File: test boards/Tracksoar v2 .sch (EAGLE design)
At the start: 53 parts, among them IC1 BME280, Y1 16MHZ

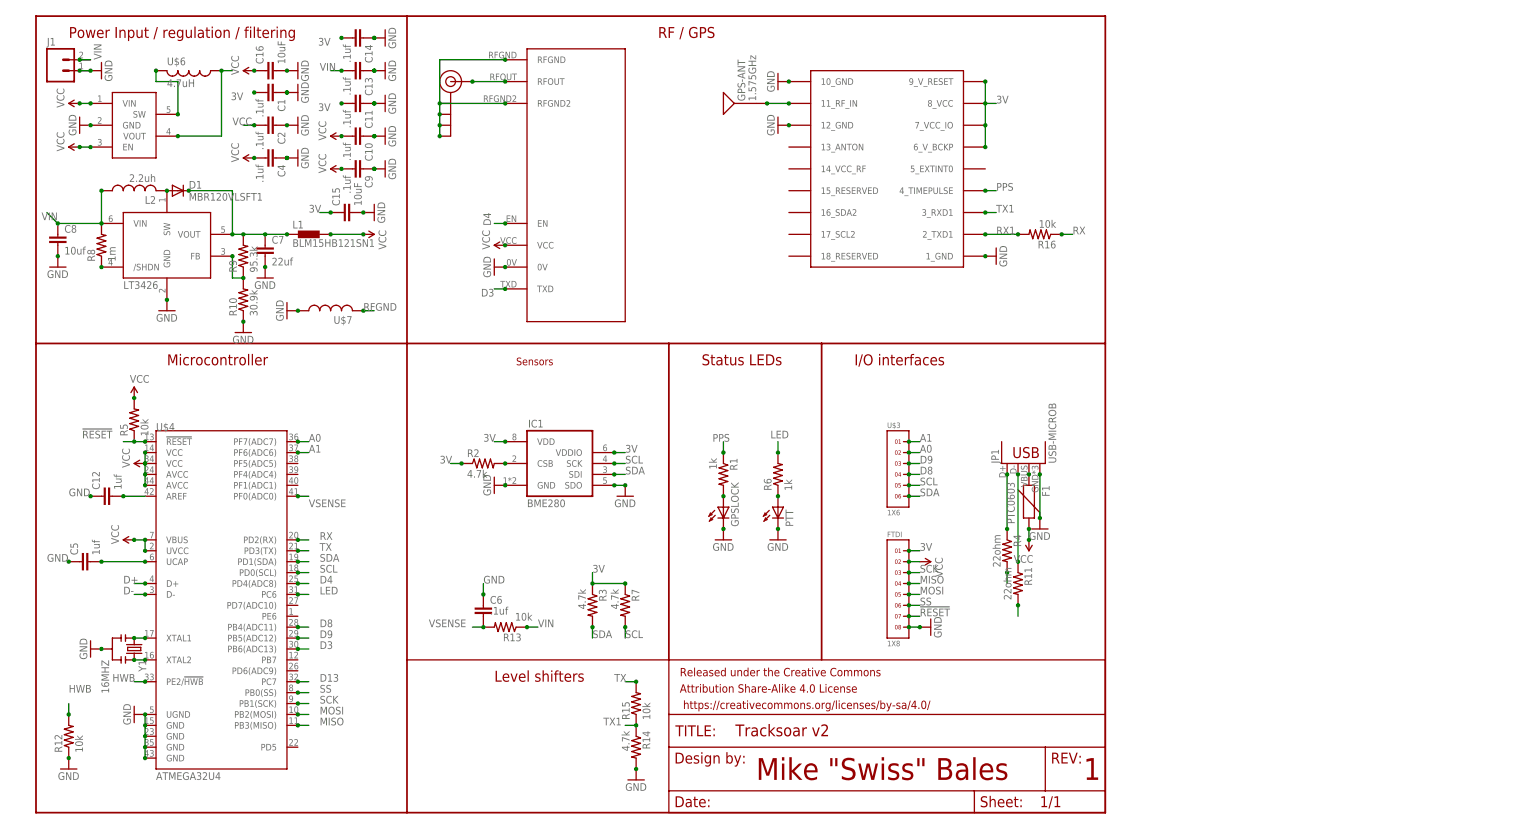
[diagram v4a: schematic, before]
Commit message: Added gps backup cap
added gps backup capacitor. Corrected serial voltage divider resistor values. Removed ground vias below gps module.
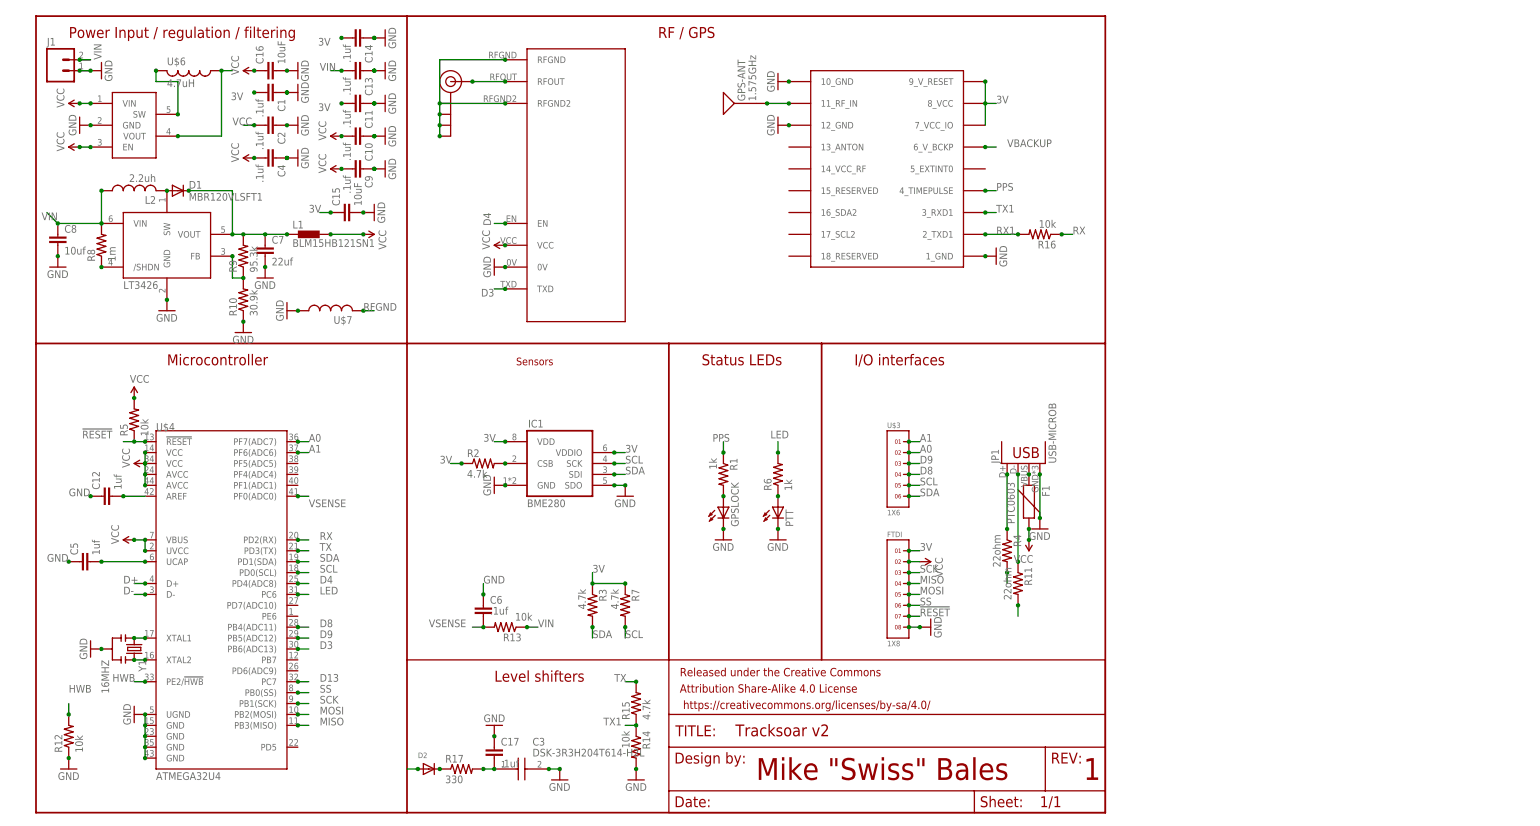
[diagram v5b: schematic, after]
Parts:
- added C17: .1uf, SparkFun-Capacitors:CAP0402-CAP
- added C3: DSK-3R3H204T614-H2L, DSK-3R3H204T614-H2L:DSK-3R3H204T614-H2L
- added D2: (no value), adafruit:DIODESOD-123
- added R17: 330, adafruit:R-US_R0402
- R14: value 4.7k -> 10k
- R15: value 10k -> 4.7k
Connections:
- new net N$22: D2.C, R17.1
- new net VBACKUP: C17.2, C3.+, R17.2, U$1.6_V_BCKP
- net 3V: now also D2.A; no longer U$1.6_V_BCKP
- net GND: now also C17.1, C3.-
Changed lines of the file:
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@@
 <part name="GND3" library="SparkFun-Aesthetics" deviceset="GND" device=""/>
 <part name="GND31" library="SparkFun-Aesthetics" deviceset="GND" device=""/>
-<part name="R14" library="adafruit" deviceset="R-US_" device="R0402" value="4.7k"/>
-<part name="R15" library="adafruit" deviceset="R-US_" device="R0402" value="10k"/>
+<part name="R14" library="adafruit" deviceset="R-US_" device="R0402" value="10k"/>
+<part name="R15" library="adafruit" deviceset="R-US_" device="R0402" value="4.7k"/>
 <part name="GND1" library="SparkFun-Aesthetics" deviceset="GND" device=""/>
 <part name="R16" library="adafruit" deviceset="R-US_" device="R0402" value="10k"/>
@@
 <part name="C2" library="SparkFun-Capacitors" deviceset="CAP" device="0402-CAP" value=".1uf"/>
 <part name="GND2" library="SparkFun-Aesthetics" deviceset="GND" device=""/>
+<part name="C3" library="DSK-3R3H204T614-H2L" deviceset="DSK-3R3H204T614-H2L" device=""/>
+<part name="D2" library="adafruit" library_urn="urn:adsk.eagle:library:420" deviceset="DIODE" device="SOD-123"/>
+<part name="R17" library="adafruit" deviceset="R-US_" device="R0402" value="330"/>
+<part name="C17" library="SparkFun-Capacitors" deviceset="CAP" device="0402-CAP" value=".1uf"/>
+<part name="GND4" library="SparkFun-Aesthetics" deviceset="GND" device=""/>
+<part name="GND33" library="SparkFun-Aesthetics" deviceset="GND" device=""/>
 </parts>
 <sheets>
@@
 <instance part="C2" gate="G$1" x="53.34" y="160.02" rot="R270"/>
 <instance part="GND2" gate="1" x="60.96" y="160.02" rot="R90"/>
+<instance part="C3" gate="G$1" x="106.68" y="10.16"/>
+<instance part="D2" gate="G$1" x="91.44" y="10.16"/>
+<instance part="R17" gate="G$1" x="99.06" y="10.16"/>
+<instance part="C17" gate="G$1" x="106.68" y="12.7"/>
+<instance part="GND4" gate="1" x="106.68" y="20.32" rot="R180"/>
+<instance part="GND33" gate="1" x="121.92" y="7.62"/>
 </instances>
 <busses>
@@
 <junction x="58.42" y="160.02"/>
 </segment>
+<segment>
+<pinref part="C3" gate="G$1" pin="-"/>
+<wire x1="119.38" y1="10.16" x2="121.92" y2="10.16" width="0.1524" layer="91"/>
+<junction x="119.38" y="10.16"/>
+<pinref part="GND33" gate="1" pin="GND"/>
+<junction x="121.92" y="10.16"/>
+</segment>
+<segment>
+<pinref part="C17" gate="G$1" pin="1"/>
+<pinref part="GND4" gate="1" pin="GND"/>
+<junction x="106.68" y="17.78"/>
+</segment>
 </net>
 <net name="D3" class="0">
@@
 <pinref part="U$1" gate="G$1" pin="7_VCC_IO"/>
 <wire x1="220.98" y1="170.18" x2="220.98" y2="165.1" width="0.1524" layer="91"/>
-<junction x="220.98" y="160.02"/>
 <junction x="220.98" y="165.1"/>
 <wire x1="220.98" y1="165.1" x2="220.98" y2="160.02" width="0.1524" layer="91"/>
 <junction x="220.98" y="170.18"/>
-<pinref part="U$1" gate="G$1" pin="6_V_BCKP"/>
-<wire x1="220.98" y1="160.02" x2="220.98" y2="154.94" width="0.1524" layer="91"/>
-<junction x="220.98" y="154.94"/>
 </segment>
 <segment>
@@
 <junction x="33.02" y="157.48"/>
 <junction x="43.18" y="172.72"/>
+</segment>
+<segment>
+<pinref part="D2" gate="G$1" pin="A"/>
+<wire x1="88.9" y1="10.16" x2="86.36" y2="10.16" width="0.1524" layer="91"/>
+<junction x="88.9" y="10.16"/>
 </segment>
 </net>
@@
 </segment>
 </net>
+<net name="VBACKUP" class="0">
+<segment>
+<pinref part="U$1" gate="G$1" pin="6_V_BCKP"/>
+<wire x1="220.98" y1="154.94" x2="223.52" y2="154.94" width="0.1524" layer="91"/>
+<label x="226.06" y="154.94" size="1.778" layer="95"/>
+<junction x="220.98" y="154.94"/>
+</segment>
+<segment>
+<pinref part="C3" gate="G$1" pin="+"/>
+<wire x1="106.68" y1="10.16" x2="104.14" y2="10.16" width="0.1524" layer="91"/>
+<junction x="106.68" y="10.16"/>
+<pinref part="R17" gate="G$1" pin="2"/>
+<junction x="104.14" y="10.16"/>
+<pinref part="C17" gate="G$1" pin="2"/>
+</segment>
+</net>
+<net name="N$22" class="0">
+<segment>
+<pinref part="R17" gate="G$1" pin="1"/>
+<pinref part="D2" gate="G$1" pin="C"/>
+<junction x="93.98" y="10.16"/>
+</segment>
+</net>

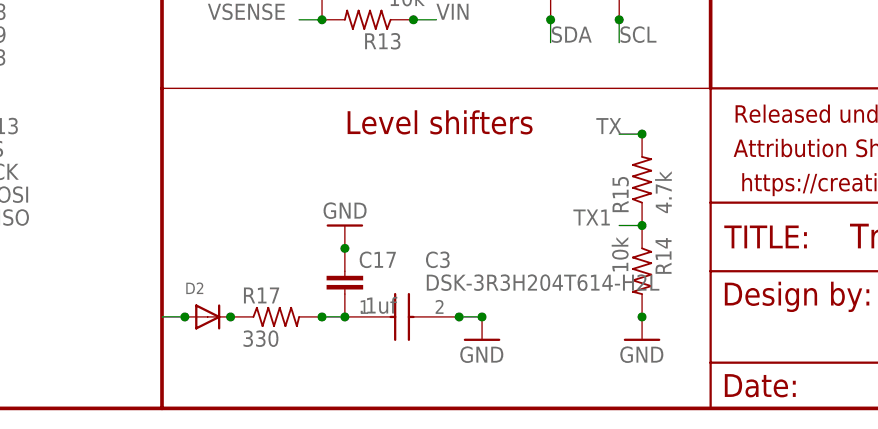
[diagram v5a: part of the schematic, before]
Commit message: Fixed airwire issue
Fixed an issue with the v2 board that resulted from upgrading eagle to v9. It caused lots of very short airwires.
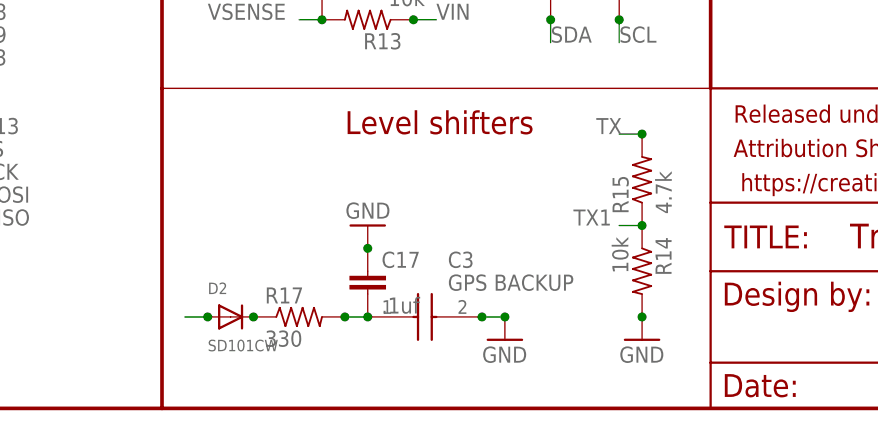
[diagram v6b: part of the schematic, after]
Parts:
- C3: value DSK-3R3H204T614-H2L -> GPS BACKUP
- D2: value (none) -> SD101CW
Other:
- moved on the sheet: C17, C3, D2, R17
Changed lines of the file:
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@@
 <?xml version="1.0" encoding="utf-8"?>
 <!DOCTYPE eagle SYSTEM "eagle.dtd">
-<eagle version="8.6.3">
+<eagle version="9.0.0">
 <drawing>
 <settings>
@@
 <part name="C2" library="SparkFun-Capacitors" deviceset="CAP" device="0402-CAP" value=".1uf"/>
 <part name="GND2" library="SparkFun-Aesthetics" deviceset="GND" device=""/>
-<part name="C3" library="DSK-3R3H204T614-H2L" deviceset="DSK-3R3H204T614-H2L" device=""/>
-<part name="D2" library="adafruit" library_urn="urn:adsk.eagle:library:420" deviceset="DIODE" device="SOD-123"/>
+<part name="C3" library="DSK-3R3H204T614-H2L" deviceset="DSK-3R3H204T614-H2L" device="" value="GPS BACKUP"/>
+<part name="D2" library="adafruit" library_urn="urn:adsk.eagle:library:420" deviceset="DIODE" device="SOD-123" value="SD101CW"/>
 <part name="R17" library="adafruit" deviceset="R-US_" device="R0402" value="330"/>
 <part name="C17" library="SparkFun-Capacitors" deviceset="CAP" device="0402-CAP" value=".1uf"/>
@@
 <instance part="C2" gate="G$1" x="53.34" y="160.02" rot="R270"/>
 <instance part="GND2" gate="1" x="60.96" y="160.02" rot="R90"/>
-<instance part="C3" gate="G$1" x="106.68" y="10.16"/>
-<instance part="D2" gate="G$1" x="91.44" y="10.16"/>
-<instance part="R17" gate="G$1" x="99.06" y="10.16"/>
-<instance part="C17" gate="G$1" x="106.68" y="12.7"/>
-<instance part="GND4" gate="1" x="106.68" y="20.32" rot="R180"/>
-<instance part="GND33" gate="1" x="121.92" y="7.62"/>
+<instance part="C3" gate="G$1" x="109.22" y="10.16"/>
+<instance part="D2" gate="G$1" x="93.98" y="10.16"/>
+<instance part="R17" gate="G$1" x="101.6" y="10.16"/>
+<instance part="C17" gate="G$1" x="109.22" y="12.7"/>
+<instance part="GND4" gate="1" x="109.22" y="20.32" rot="R180"/>
+<instance part="GND33" gate="1" x="124.46" y="7.62"/>
 </instances>
 <busses>
@@
 <segment>
 <pinref part="C3" gate="G$1" pin="-"/>
-<wire x1="119.38" y1="10.16" x2="121.92" y2="10.16" width="0.1524" layer="91"/>
-<junction x="119.38" y="10.16"/>
+<wire x1="121.92" y1="10.16" x2="124.46" y2="10.16" width="0.1524" layer="91"/>
+<junction x="121.92" y="10.16"/>
 <pinref part="GND33" gate="1" pin="GND"/>
-<junction x="121.92" y="10.16"/>
+<junction x="124.46" y="10.16"/>
 </segment>
 <segment>
 <pinref part="C17" gate="G$1" pin="1"/>
 <pinref part="GND4" gate="1" pin="GND"/>
-<junction x="106.68" y="17.78"/>
+<junction x="109.22" y="17.78"/>
 </segment>
 </net>
@@
 <segment>
 <pinref part="D2" gate="G$1" pin="A"/>
-<wire x1="88.9" y1="10.16" x2="86.36" y2="10.16" width="0.1524" layer="91"/>
-<junction x="88.9" y="10.16"/>
+<wire x1="91.44" y1="10.16" x2="88.9" y2="10.16" width="0.1524" layer="91"/>
+<junction x="91.44" y="10.16"/>
 </segment>
 </net>
@@
 <segment>
 <pinref part="C3" gate="G$1" pin="+"/>
-<wire x1="106.68" y1="10.16" x2="104.14" y2="10.16" width="0.1524" layer="91"/>
+<wire x1="109.22" y1="10.16" x2="106.68" y2="10.16" width="0.1524" layer="91"/>
+<junction x="109.22" y="10.16"/>
+<pinref part="R17" gate="G$1" pin="2"/>
 <junction x="106.68" y="10.16"/>
-<pinref part="R17" gate="G$1" pin="2"/>
-<junction x="104.14" y="10.16"/>
 <pinref part="C17" gate="G$1" pin="2"/>
 </segment>
@@
 <pinref part="R17" gate="G$1" pin="1"/>
 <pinref part="D2" gate="G$1" pin="C"/>
-<junction x="93.98" y="10.16"/>
-</segment>
-</net>
+<junction x="96.52" y="10.16"/>
+</segment>
+</net>

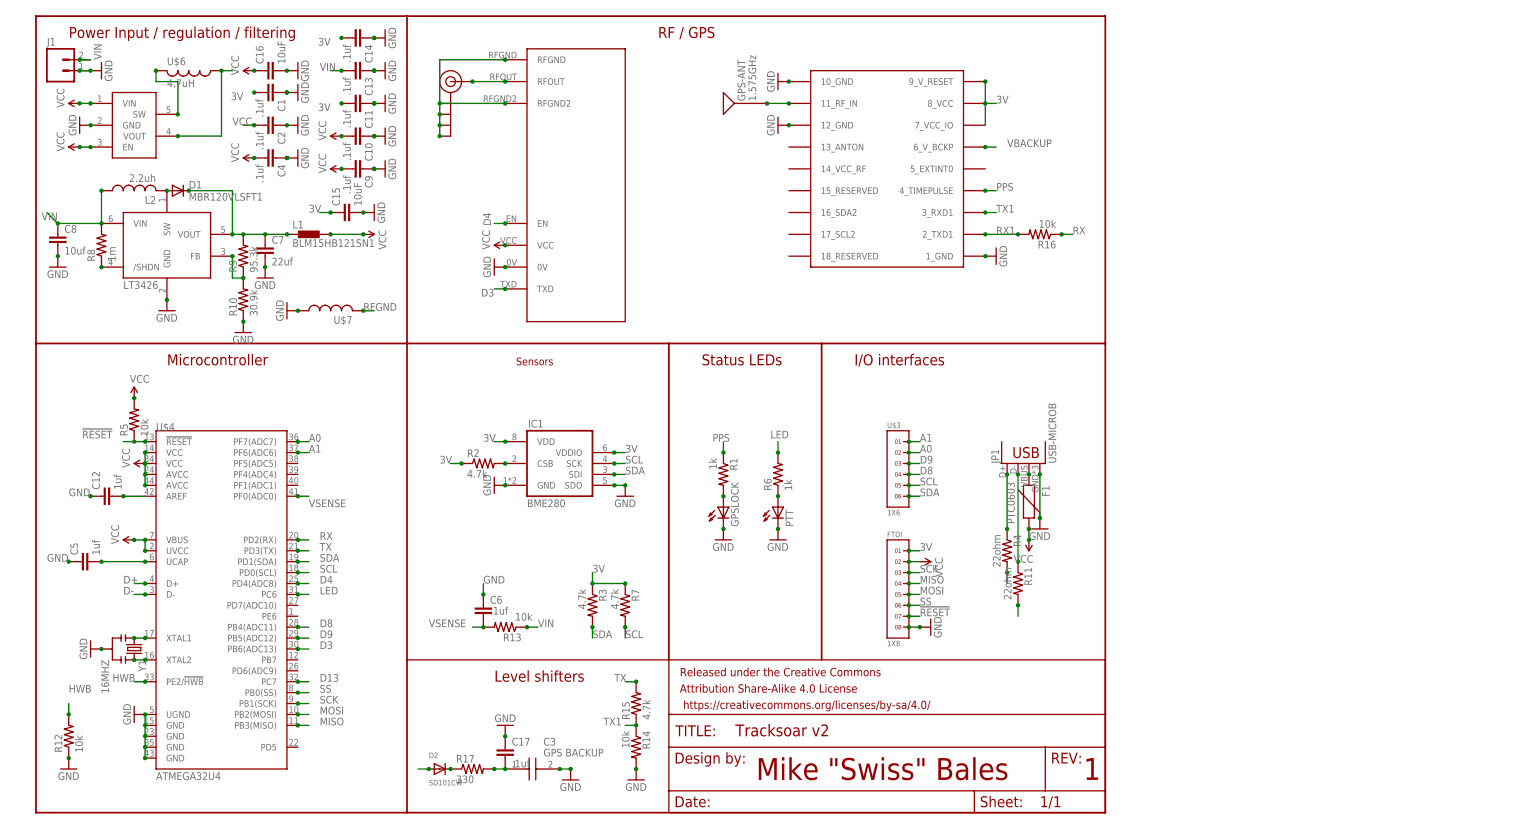
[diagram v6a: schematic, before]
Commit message: Schematic cleanup
first pass at making the schematic more readable. Moved components to be more in line with the board layout.
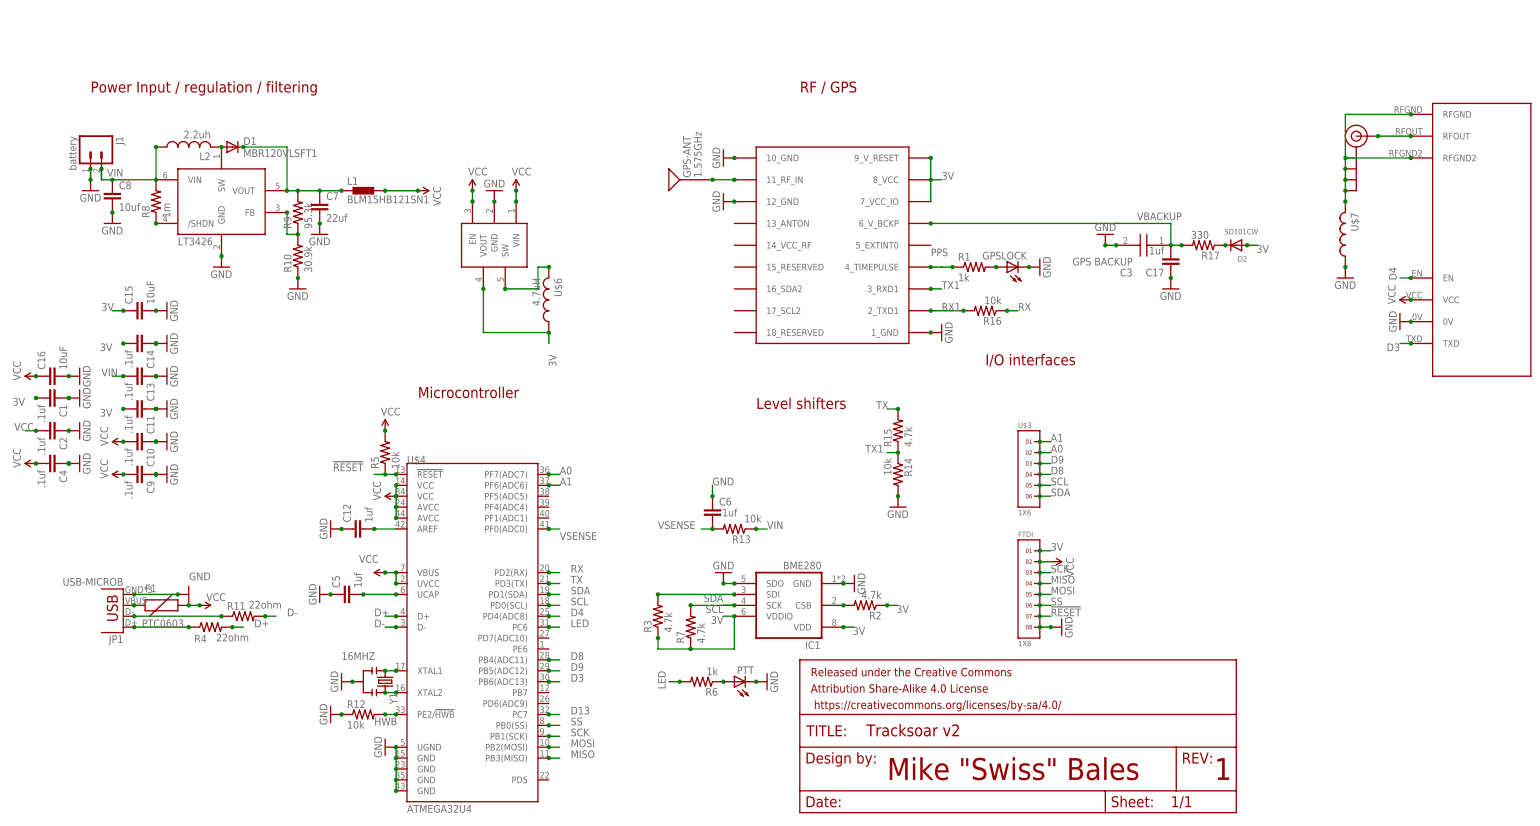
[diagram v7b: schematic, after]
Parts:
- J1: value (none) -> battery
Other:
- note removed: "Sensors"
- note removed: "Status LEDs"
- moved on the sheet: C1, C10, C11, C12, C13, C14, C15, C16, C17, C2, C3, C4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

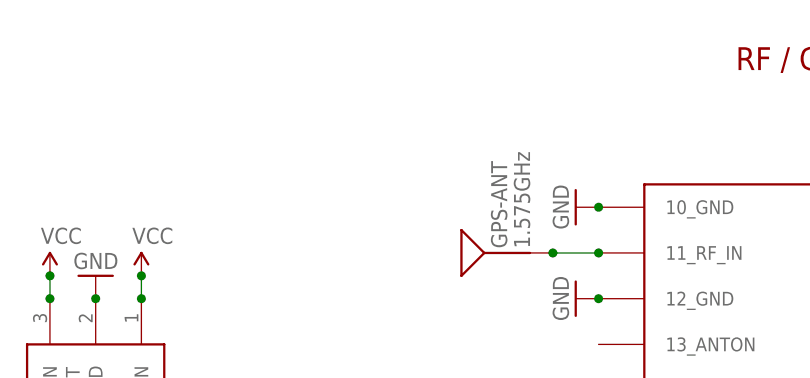
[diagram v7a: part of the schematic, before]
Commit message: added breakout mount holes
added 2.8mm mounting holes with mouse bites for easy removal.
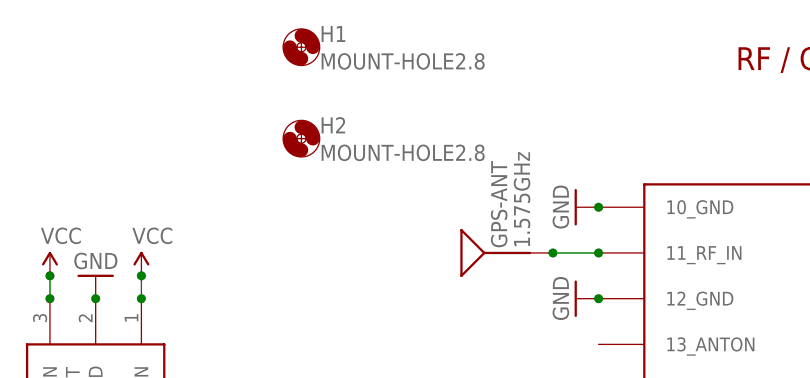
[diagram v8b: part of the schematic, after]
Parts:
- added H1, H2: MOUNT-HOLE2.8, holes:MOUNT-HOLE2.8
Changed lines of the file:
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@@
 <part name="GND34" library="SparkFun-Aesthetics" deviceset="GND" device=""/>
 <part name="GND35" library="SparkFun-Aesthetics" deviceset="GND" device=""/>
+<part name="H1" library="holes" library_urn="urn:adsk.eagle:library:237" deviceset="MOUNT-HOLE" device="2.8" package3d_urn="urn:adsk.eagle:package:14271/1" value="MOUNT-HOLE2.8"/>
+<part name="H2" library="holes" library_urn="urn:adsk.eagle:library:237" deviceset="MOUNT-HOLE" device="2.8" package3d_urn="urn:adsk.eagle:package:14271/1" value="MOUNT-HOLE2.8"/>
 </parts>
 <sheets>
@@
 <instance part="GND34" gate="1" x="68.58" y="66.04" rot="R270"/>
 <instance part="GND35" gate="1" x="66.04" y="50.8" rot="R270"/>
+<instance part="H1" gate="G$1" x="129.54" y="170.18"/>
+<instance part="H2" gate="G$1" x="129.54" y="160.02"/>
 </instances>
 <busses>
